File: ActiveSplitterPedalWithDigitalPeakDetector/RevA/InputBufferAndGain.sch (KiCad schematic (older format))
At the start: 7 parts, among them U2 TL072

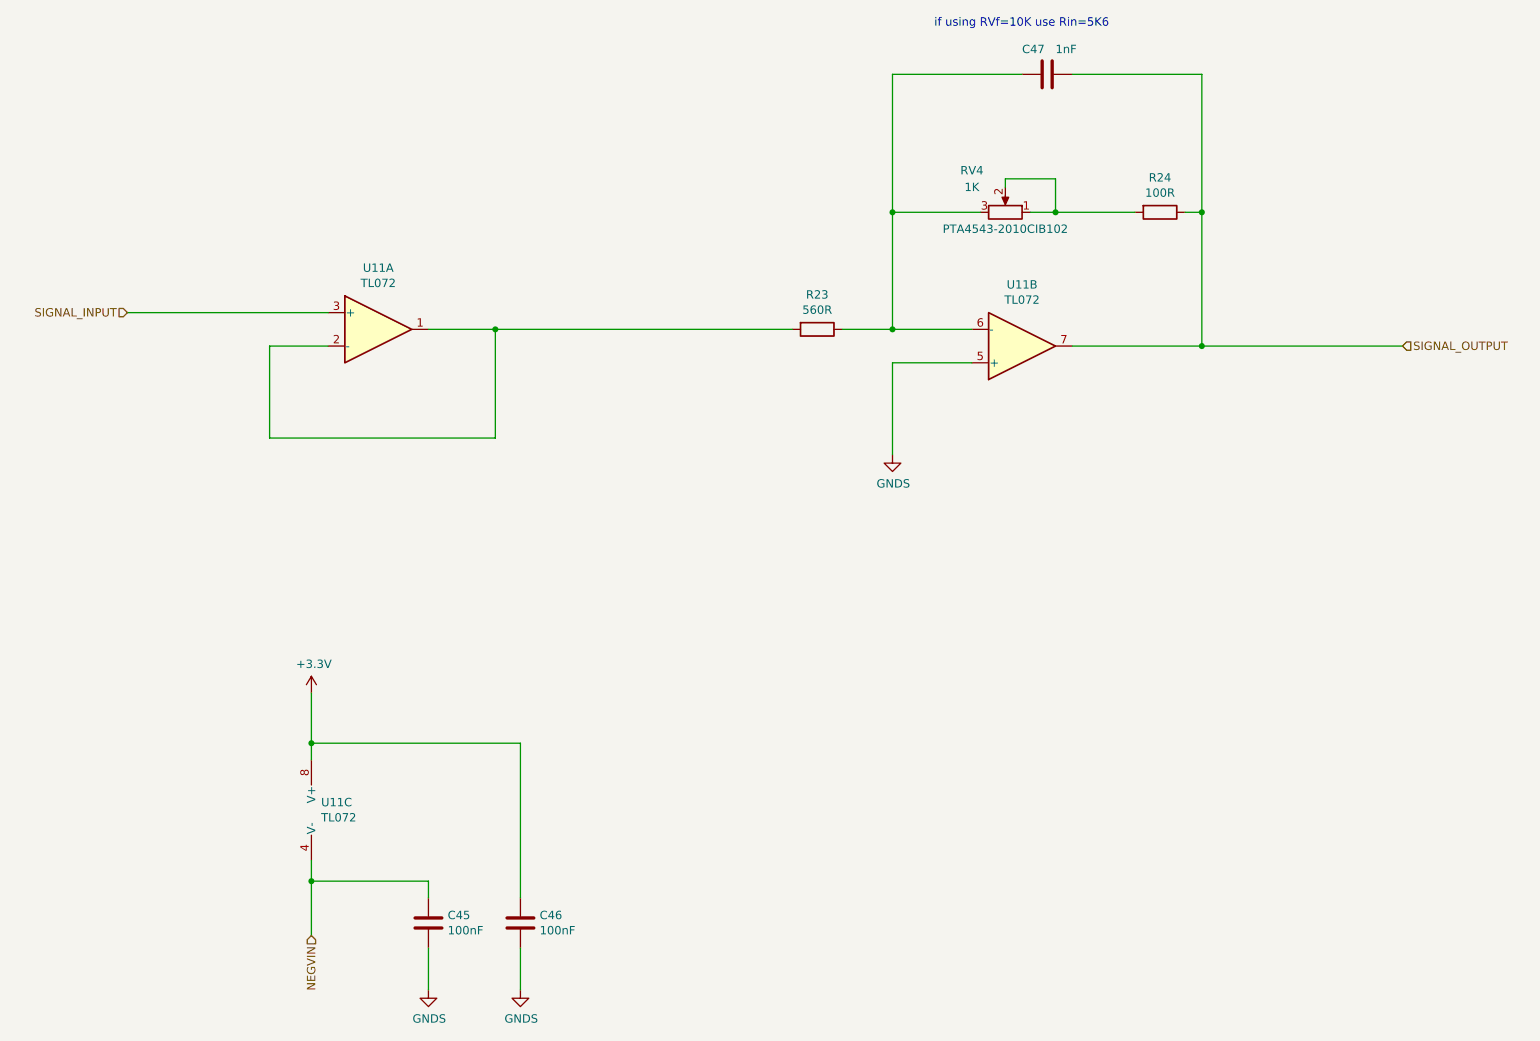
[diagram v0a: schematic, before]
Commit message: hw update
moved led resistors to back copper layer
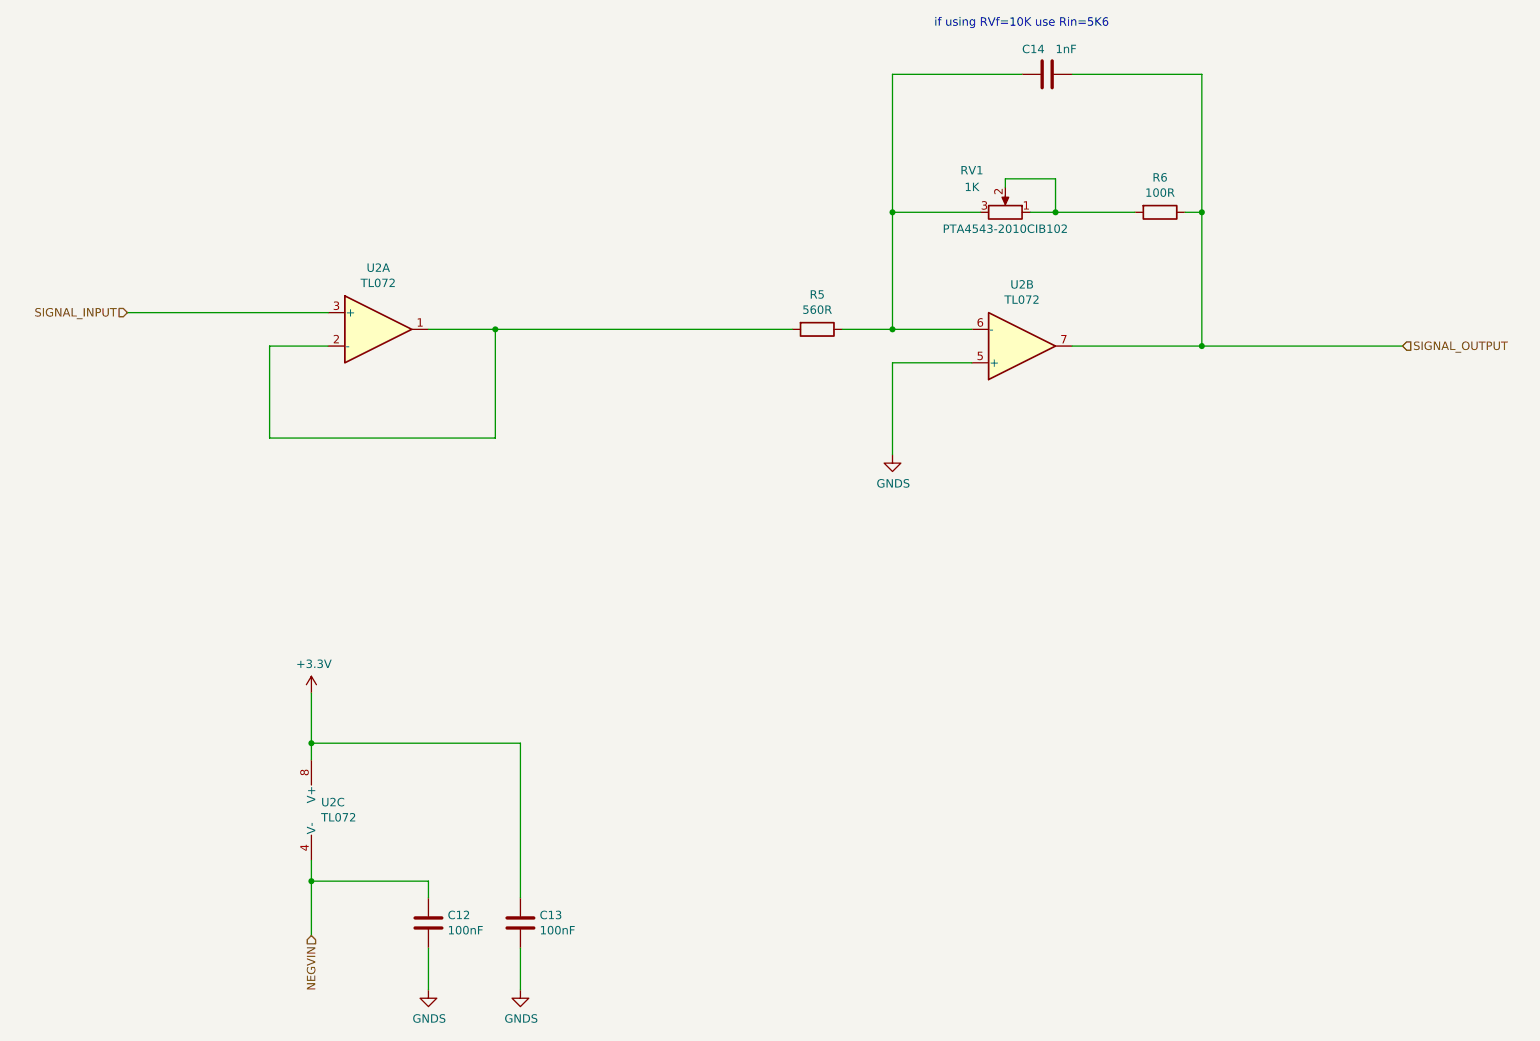
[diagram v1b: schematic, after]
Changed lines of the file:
@@
 $Descr A4 11693 8268
 encoding utf-8
-Sheet 4 15
+Sheet 2 15
 Title ""
 Date ""
@@
 AR Path="/5F6A445C/5F59292E" Ref="R17"  Part="1"
 AR Path="/5F6AEF24/5F59292E" Ref="R23"  Part="1"
-F 0 "R23" V 6018 2875 50  0000 C CNN
+F 0 "R5" V 6018 2875 50  0000 C CNN
 F 1 "560R" V 6109 2875 50  0000 C CNN
 F 2 "Resistor_SMD:R_0805_2012Metric_Pad1.15x1.40mm_HandSolder" V 6155 2875 50  0001 C CNN
@@
 AR Path="/5F6A445C/5F59293F" Ref="RV3"  Part="1"
 AR Path="/5F6AEF24/5F59293F" Ref="RV4"  Part="1"
-F 0 "RV4" V 7600 1975 50  0000 C CNN
+F 0 "RV1" V 7600 1975 50  0000 C CNN
 F 1 "1K" V 7500 1975 50  0000 C CNN
 F 2 "Bourn_PTA_Slider:Slider_PTA4543_60MM" H 7350 2175 50  0001 C CNN
@@
 AR Path="/5F6A445C/5F592956" Ref="R18"  Part="1"
 AR Path="/5F6AEF24/5F592956" Ref="R24"  Part="1"
-F 0 "R24" V 8068 2175 50  0000 C CNN
+F 0 "R6" V 8068 2175 50  0000 C CNN
 F 1 "100R" V 8159 2175 50  0000 C CNN
 F 2 "Resistor_SMD:R_0805_2012Metric_Pad1.15x1.40mm_HandSolder" V 8205 2175 50  0001 C CNN
@@
 AR Path="/5F6A445C/5F59295D" Ref="C36"  Part="1"
 AR Path="/5F6AEF24/5F59295D" Ref="C47"  Part="1"
-F 0 "C47" V 7450 1200 50  0000 L CNN
+F 0 "C14" V 7450 1200 50  0000 L CNN
 F 1 "1nF" V 7450 1400 50  0000 L CNN
 F 2 "Capacitor_SMD:C_0805_2012Metric_Pad1.15x1.40mm_HandSolder" H 7638 1200 50  0001 C CNN
@@
 AR Path="/5F6A445C/5F59AE7C" Ref="U8"  Part="1"
 AR Path="/5F6AEF24/5F59AE7C" Ref="U11"  Part="1"
-F 0 "U11" H 3600 3242 50  0000 C CNN
+F 0 "U2" H 3600 3242 50  0000 C CNN
 F 1 "TL072" H 3600 3151 50  0000 C CNN
 F 2 "Package_SO:SOIC-8_3.9x4.9mm_P1.27mm" H 3600 2875 50  0001 C CNN
@@
 AR Path="/5F6A445C/5F59C9C2" Ref="U8"  Part="2"
 AR Path="/5F6AEF24/5F59C9C2" Ref="U11"  Part="2"
-F 0 "U11" H 7450 2608 50  0000 C CNN
+F 0 "U2" H 7450 2608 50  0000 C CNN
 F 1 "TL072" H 7450 2699 50  0000 C CNN
 F 2 "Package_SO:SOIC-8_3.9x4.9mm_P1.27mm" H 7450 2975 50  0001 C CNN
@@
 AR Path="/5F6A445C/5F59E5A5" Ref="U8"  Part="3"
 AR Path="/5F6AEF24/5F59E5A5" Ref="U11"  Part="3"
-F 0 "U11" H 3258 5796 50  0000 L CNN
+F 0 "U2" H 3258 5796 50  0000 L CNN
 F 1 "TL072" H 3258 5705 50  0000 L CNN
 F 2 "Package_SO:SOIC-8_3.9x4.9mm_P1.27mm" H 3300 5750 50  0001 C CNN
@@
 AR Path="/5F6A445C/5F5D3555" Ref="C34"  Part="1"
 AR Path="/5F6AEF24/5F5D3555" Ref="C45"  Part="1"
-F 0 "C45" H 4015 6471 50  0000 L CNN
+F 0 "C12" H 4015 6471 50  0000 L CNN
 F 1 "100nF" H 4015 6380 50  0000 L CNN
 F 2 "Capacitor_SMD:C_0805_2012Metric_Pad1.15x1.40mm_HandSolder" H 3938 6275 50  0001 C CNN
@@
 AR Path="/5F6A445C/5F5D446F" Ref="C35"  Part="1"
 AR Path="/5F6AEF24/5F5D446F" Ref="C46"  Part="1"
-F 0 "C46" H 4565 6471 50  0000 L CNN
+F 0 "C13" H 4565 6471 50  0000 L CNN
 F 1 "100nF" H 4565 6380 50  0000 L CNN
 F 2 "Capacitor_SMD:C_0805_2012Metric_Pad1.15x1.40mm_HandSolder" H 4488 6275 50  0001 C CNN
@@
 AR Path="/5F6A445C/5F596316" Ref="#PWR0139"  Part="1"
 AR Path="/5F6AEF24/5F596316" Ref="#PWR0151"  Part="1"
-F 0 "#PWR0151" H 3200 4900 50  0001 C CNN
+F 0 "#PWR0115" H 3200 4900 50  0001 C CNN
 F 1 "+3.3V" H 3215 5223 50  0000 C CNN
 F 2 "" H 3200 5050 50  0001 C CNN
@@
 AR Path="/5F6A445C/5F6D90B6" Ref="#PWR0108"  Part="1"
 AR Path="/5F6AEF24/5F6D90B6" Ref="#PWR0109"  Part="1"
-F 0 "#PWR0109" H 6675 3375 50  0001 C CNN
+F 0 "#PWR0106" H 6675 3375 50  0001 C CNN
 F 1 "GNDS" H 6680 3452 50  0000 C CNN
 F 2 "" H 6675 3625 50  0001 C CNN
@@
 AR Path="/5F6A445C/5F838592" Ref="#PWR0118"  Part="1"
 AR Path="/5F6AEF24/5F838592" Ref="#PWR0120"  Part="1"
-F 0 "#PWR0120" H 3900 6575 50  0001 C CNN
+F 0 "#PWR0111" H 3900 6575 50  0001 C CNN
 F 1 "GNDS" H 3905 6652 50  0000 C CNN
 F 2 "" H 3900 6825 50  0001 C CNN
@@
 AR Path="/5F6A445C/5F838D32" Ref="#PWR0119"  Part="1"
 AR Path="/5F6AEF24/5F838D32" Ref="#PWR0121"  Part="1"
-F 0 "#PWR0121" H 4450 6575 50  0001 C CNN
+F 0 "#PWR0112" H 4450 6575 50  0001 C CNN
 F 1 "GNDS" H 4455 6652 50  0000 C CNN
 F 2 "" H 4450 6825 50  0001 C CNN

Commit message: schematic update
updated resistor (Rin) to 1K/10K
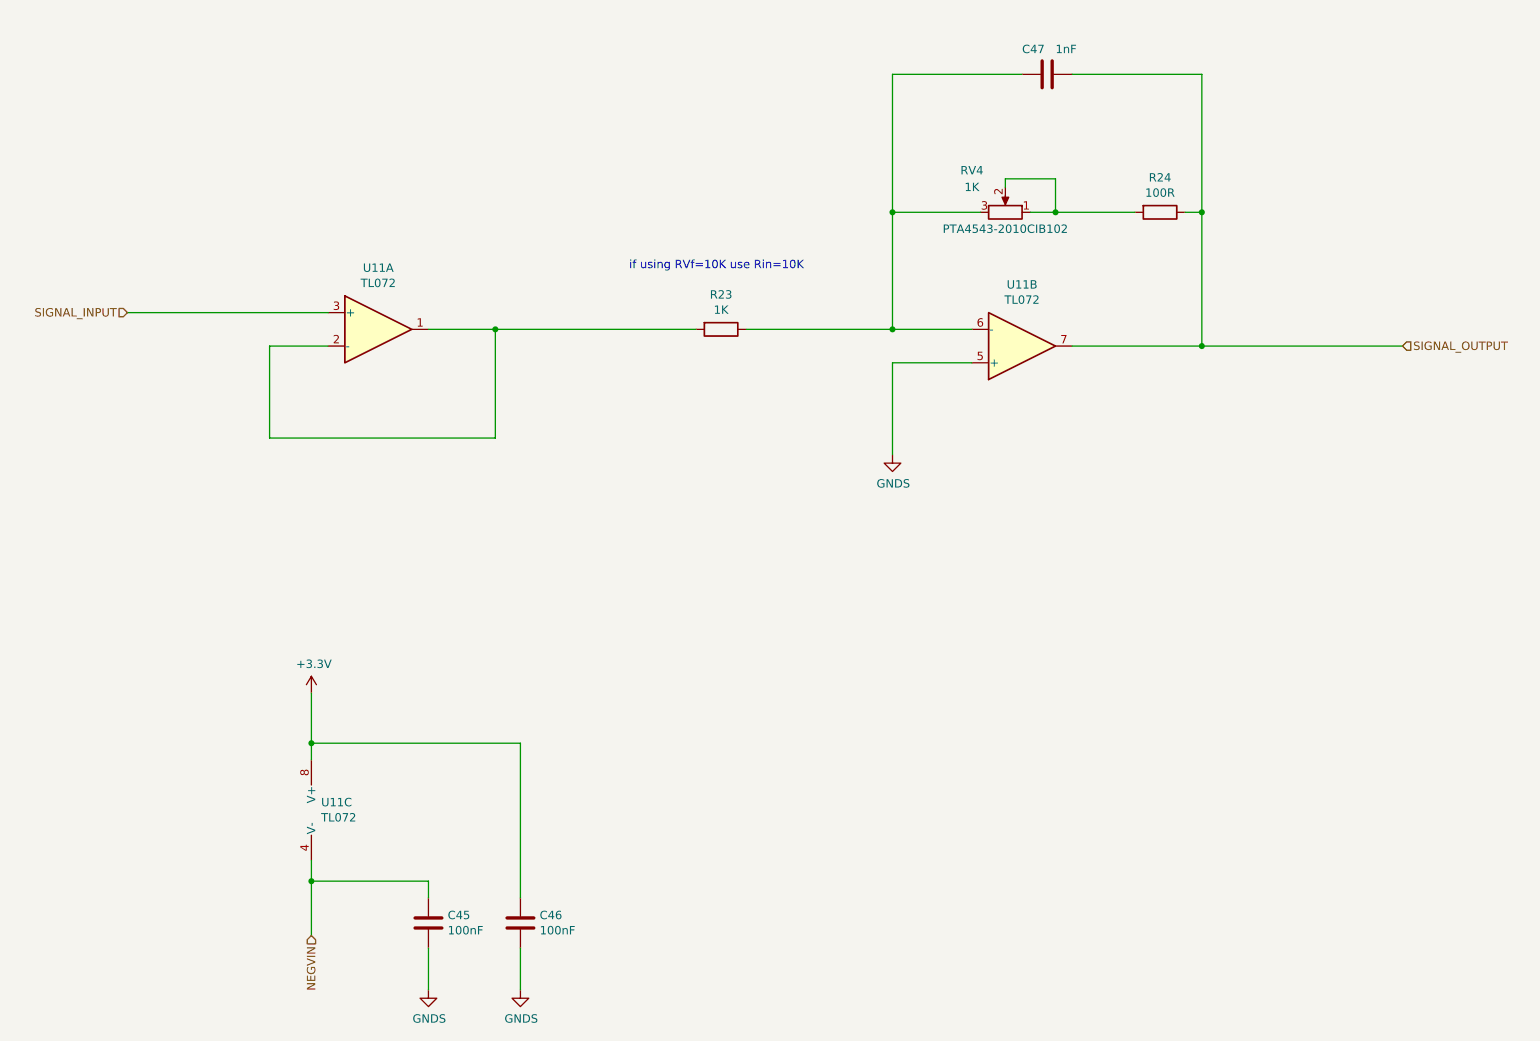
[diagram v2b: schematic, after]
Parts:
- R5: value 560R -> 1K
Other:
- note added: "if using RVf=10K use Rin=10K\n"
- note removed: "if using RVf=10K use Rin=5K6"
- moved on the sheet: R23
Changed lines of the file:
@@
 $Descr A4 11693 8268
 encoding utf-8
-Sheet 2 15
+Sheet 5 15
 Title ""
 Date ""
@@
 L Device:R R?
 U 1 1 5F59292E
-P 6225 2875
+P 5650 2875
 AR Path="/5F3F1F31/5F59292E" Ref="R?"  Part="1"
 AR Path="/5F512144/5F59292E" Ref="R?"  Part="1"
@@
 AR Path="/5F6A445C/5F59292E" Ref="R17"  Part="1"
 AR Path="/5F6AEF24/5F59292E" Ref="R23"  Part="1"
-F 0 "R5" V 6018 2875 50  0000 C CNN
-F 1 "560R" V 6109 2875 50  0000 C CNN
-F 2 "Resistor_SMD:R_0805_2012Metric_Pad1.15x1.40mm_HandSolder" V 6155 2875 50  0001 C CNN
-F 3 "~" H 6225 2875 50  0001 C CNN
-	1    6225 2875
+F 0 "R23" V 5443 2875 50  0000 C CNN
+F 1 "1K" V 5534 2875 50  0000 C CNN
+F 2 "Resistor_SMD:R_0805_2012Metric_Pad1.15x1.40mm_HandSolder" V 5580 2875 50  0001 C CNN
+F 3 "~" H 5650 2875 50  0001 C CNN
+	1    5650 2875
 	0    1    1    0
 $EndComp
@@
 AR Path="/5F6A445C/5F59293F" Ref="RV3"  Part="1"
 AR Path="/5F6AEF24/5F59293F" Ref="RV4"  Part="1"
-F 0 "RV1" V 7600 1975 50  0000 C CNN
+F 0 "RV4" V 7600 1975 50  0000 C CNN
 F 1 "1K" V 7500 1975 50  0000 C CNN
 F 2 "Bourn_PTA_Slider:Slider_PTA4543_60MM" H 7350 2175 50  0001 C CNN
@@
 Connection ~ 6675 2875
 Wire Wire Line
-	6675 2875 6375 2875
+	6675 2875 5800 2875
 Wire Wire Line
 	8525 2975 9725 2975
-Text Notes 6925 1075 0    50   ~ 0
-if using RVf=10K use Rin=5K6
+Text Notes 5100 2525 0    50   ~ 0
+if using RVf=10K use Rin=10K\n
 Connection ~ 8525 2975
 Wire Wire Line
@@
 AR Path="/5F6A445C/5F592956" Ref="R18"  Part="1"
 AR Path="/5F6AEF24/5F592956" Ref="R24"  Part="1"
-F 0 "R6" V 8068 2175 50  0000 C CNN
+F 0 "R24" V 8068 2175 50  0000 C CNN
 F 1 "100R" V 8159 2175 50  0000 C CNN
 F 2 "Resistor_SMD:R_0805_2012Metric_Pad1.15x1.40mm_HandSolder" V 8205 2175 50  0001 C CNN
@@
 AR Path="/5F6A445C/5F59295D" Ref="C36"  Part="1"
 AR Path="/5F6AEF24/5F59295D" Ref="C47"  Part="1"
-F 0 "C14" V 7450 1200 50  0000 L CNN
+F 0 "C47" V 7450 1200 50  0000 L CNN
 F 1 "1nF" V 7450 1400 50  0000 L CNN
 F 2 "Capacitor_SMD:C_0805_2012Metric_Pad1.15x1.40mm_HandSolder" H 7638 1200 50  0001 C CNN
@@
 Connection ~ 8525 2175
 Wire Wire Line
-	4300 2875 6075 2875
+	4300 2875 5500 2875
 $Comp
 L Amplifier_Operational:TL072 U2
@@
 AR Path="/5F6A445C/5F59AE7C" Ref="U8"  Part="1"
 AR Path="/5F6AEF24/5F59AE7C" Ref="U11"  Part="1"
-F 0 "U2" H 3600 3242 50  0000 C CNN
+F 0 "U11" H 3600 3242 50  0000 C CNN
 F 1 "TL072" H 3600 3151 50  0000 C CNN
 F 2 "Package_SO:SOIC-8_3.9x4.9mm_P1.27mm" H 3600 2875 50  0001 C CNN
@@
 AR Path="/5F6A445C/5F59C9C2" Ref="U8"  Part="2"
 AR Path="/5F6AEF24/5F59C9C2" Ref="U11"  Part="2"
-F 0 "U2" H 7450 2608 50  0000 C CNN
+F 0 "U11" H 7450 2608 50  0000 C CNN
 F 1 "TL072" H 7450 2699 50  0000 C CNN
 F 2 "Package_SO:SOIC-8_3.9x4.9mm_P1.27mm" H 7450 2975 50  0001 C CNN
@@
 AR Path="/5F6A445C/5F59E5A5" Ref="U8"  Part="3"
 AR Path="/5F6AEF24/5F59E5A5" Ref="U11"  Part="3"
-F 0 "U2" H 3258 5796 50  0000 L CNN
+F 0 "U11" H 3258 5796 50  0000 L CNN
 F 1 "TL072" H 3258 5705 50  0000 L CNN
 F 2 "Package_SO:SOIC-8_3.9x4.9mm_P1.27mm" H 3300 5750 50  0001 C CNN
@@
 AR Path="/5F6A445C/5F5D3555" Ref="C34"  Part="1"
 AR Path="/5F6AEF24/5F5D3555" Ref="C45"  Part="1"
-F 0 "C12" H 4015 6471 50  0000 L CNN
+F 0 "C45" H 4015 6471 50  0000 L CNN
 F 1 "100nF" H 4015 6380 50  0000 L CNN
 F 2 "Capacitor_SMD:C_0805_2012Metric_Pad1.15x1.40mm_HandSolder" H 3938 6275 50  0001 C CNN
@@
 AR Path="/5F6A445C/5F5D446F" Ref="C35"  Part="1"
 AR Path="/5F6AEF24/5F5D446F" Ref="C46"  Part="1"
-F 0 "C13" H 4565 6471 50  0000 L CNN
+F 0 "C46" H 4565 6471 50  0000 L CNN
 F 1 "100nF" H 4565 6380 50  0000 L CNN
 F 2 "Capacitor_SMD:C_0805_2012Metric_Pad1.15x1.40mm_HandSolder" H 4488 6275 50  0001 C CNN
@@
 AR Path="/5F6A445C/5F596316" Ref="#PWR0139"  Part="1"
 AR Path="/5F6AEF24/5F596316" Ref="#PWR0151"  Part="1"
-F 0 "#PWR0115" H 3200 4900 50  0001 C CNN
+F 0 "#PWR0151" H 3200 4900 50  0001 C CNN
 F 1 "+3.3V" H 3215 5223 50  0000 C CNN
 F 2 "" H 3200 5050 50  0001 C CNN
@@
 AR Path="/5F6A445C/5F6D90B6" Ref="#PWR0108"  Part="1"
 AR Path="/5F6AEF24/5F6D90B6" Ref="#PWR0109"  Part="1"
-F 0 "#PWR0106" H 6675 3375 50  0001 C CNN
+F 0 "#PWR0109" H 6675 3375 50  0001 C CNN
 F 1 "GNDS" H 6680 3452 50  0000 C CNN
 F 2 "" H 6675 3625 50  0001 C CNN
@@
 AR Path="/5F6A445C/5F838592" Ref="#PWR0118"  Part="1"
 AR Path="/5F6AEF24/5F838592" Ref="#PWR0120"  Part="1"
-F 0 "#PWR0111" H 3900 6575 50  0001 C CNN
+F 0 "#PWR0120" H 3900 6575 50  0001 C CNN
 F 1 "GNDS" H 3905 6652 50  0000 C CNN
 F 2 "" H 3900 6825 50  0001 C CNN
@@
 AR Path="/5F6A445C/5F838D32" Ref="#PWR0119"  Part="1"
 AR Path="/5F6AEF24/5F838D32" Ref="#PWR0121"  Part="1"
-F 0 "#PWR0112" H 4450 6575 50  0001 C CNN
+F 0 "#PWR0121" H 4450 6575 50  0001 C CNN
 F 1 "GNDS" H 4455 6652 50  0000 C CNN
 F 2 "" H 4450 6825 50  0001 C CNN
